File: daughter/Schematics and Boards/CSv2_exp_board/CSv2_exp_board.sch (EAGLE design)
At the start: 100 parts, among them J1 HIROSE-DF40_44-PIN_CONNECTORS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, J2 J-SERIAL-PORT, J3 CORTEX_DEBUG_SMD, J301 HIROSE-DF40_44-PIN_CONNECTORS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, J7 J-USB-HIROSE-MICRO-USB, SW1 SPST_TACT-KMR2, SW2 SPST_TACT-KMR2, U1 LOADSWITCH-MIC94164, U10 LOADSWITCH-MIC94164, U11 BMI160, U2 ADA4841-1YRJZ-R7, U205 MPL3115A2, U3 Value, U4 RFM69HCW, U5 Value, U6 Value, U7 LOADSWITCH-MIC94164, U8 LOADSWITCH-MIC94164, U9 LOADSWITCH-MIC94164, X1 32.768kHz, X2 32.768, X4 uFL

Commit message: DTR-routing 100% + DRC resolved
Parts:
- added EN_RADIO, MEAS_MIC, MEAS_RFM, MEAS_SAMD: TPTP10SQ, TestPoints:TPTP10SQ
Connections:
- net EN_RADIO: now also EN_RADIO.TP
- net MEAS_MIC: now also MEAS_MIC.TP
- net MEAS_RFM: now also MEAS_RFM.TP
- net MEAS_SAMD: now also MEAS_SAMD.TP
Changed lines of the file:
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@@
 <part name="SW1" library="adafruit" deviceset="SPST_TACT" device="-KMR2"/>
 <part name="SW2" library="adafruit" deviceset="SPST_TACT" device="-KMR2"/>
+<part name="MEAS_RFM" library="TestPoints" deviceset="TP" device="TP10SQ" package3d_urn="urn:adsk.eagle:package:27962/1" value="TPTP10SQ"/>
+<part name="MEAS_SAMD" library="TestPoints" deviceset="TP" device="TP10SQ" package3d_urn="urn:adsk.eagle:package:27962/1" value="TPTP10SQ"/>
+<part name="MEAS_MIC" library="TestPoints" deviceset="TP" device="TP10SQ" package3d_urn="urn:adsk.eagle:package:27962/1" value="TPTP10SQ"/>
+<part name="EN_RADIO" library="TestPoints" deviceset="TP" device="TP10SQ" package3d_urn="urn:adsk.eagle:package:27962/1" value="TPTP10SQ"/>
 </parts>
 <sheets>
@@
 <attribute name="VALUE" x="184.15" y="227.965" size="1.778" layer="96" rot="R270"/>
 </instance>
+<instance part="MEAS_RFM" gate="G$1" x="205.74" y="101.6" smashed="yes">
+<attribute name="NAME" x="204.47" y="102.87" size="1.778" layer="95"/>
+<attribute name="TP_SIGNAL_NAME" x="207.01" y="100.33" size="1.778" layer="97"/>
+</instance>
+<instance part="MEAS_SAMD" gate="G$1" x="208.28" y="99.06" smashed="yes">
+<attribute name="NAME" x="207.01" y="100.33" size="1.778" layer="95"/>
+<attribute name="TP_SIGNAL_NAME" x="209.55" y="97.79" size="1.778" layer="97"/>
+</instance>
+<instance part="MEAS_MIC" gate="G$1" x="203.2" y="91.44" smashed="yes">
+<attribute name="NAME" x="201.93" y="92.71" size="1.778" layer="95"/>
+<attribute name="TP_SIGNAL_NAME" x="204.47" y="90.17" size="1.778" layer="97"/>
+</instance>
+<instance part="EN_RADIO" gate="G$1" x="205.74" y="88.9" smashed="yes">
+<attribute name="NAME" x="204.47" y="90.17" size="1.778" layer="95"/>
+<attribute name="TP_SIGNAL_NAME" x="207.01" y="87.63" size="1.778" layer="97"/>
+</instance>
 </instances>
 <busses>
@@
 <wire x1="203.2" y1="88.9" x2="185.42" y2="88.9" width="0.1524" layer="91"/>
 <junction x="185.42" y="88.9"/>
+<pinref part="MEAS_MIC" gate="G$1" pin="TP"/>
 </segment>
 </net>
@@
 <wire x1="208.28" y1="96.52" x2="177.8" y2="96.52" width="0.1524" layer="91"/>
 <junction x="177.8" y="96.52"/>
+<pinref part="MEAS_SAMD" gate="G$1" pin="TP"/>
 </segment>
 </net>
@@
 <wire x1="205.74" y1="99.06" x2="175.26" y2="99.06" width="0.1524" layer="91"/>
 <junction x="175.26" y="99.06"/>
+<pinref part="MEAS_RFM" gate="G$1" pin="TP"/>
 </segment>
 </net>
@@
 <wire x1="205.74" y1="86.36" x2="187.96" y2="86.36" width="0.1524" layer="91"/>
 <junction x="187.96" y="86.36"/>
+<pinref part="EN_RADIO" gate="G$1" pin="TP"/>
 </segment>
 </net>
@@
 </segment>
 </net>
-<net name="+3V3_DTR" class="3">
+<net name="+3V3_DTR" class="0">
 <segment>
 <pinref part="J301" gate="G$1" pin="4"/>

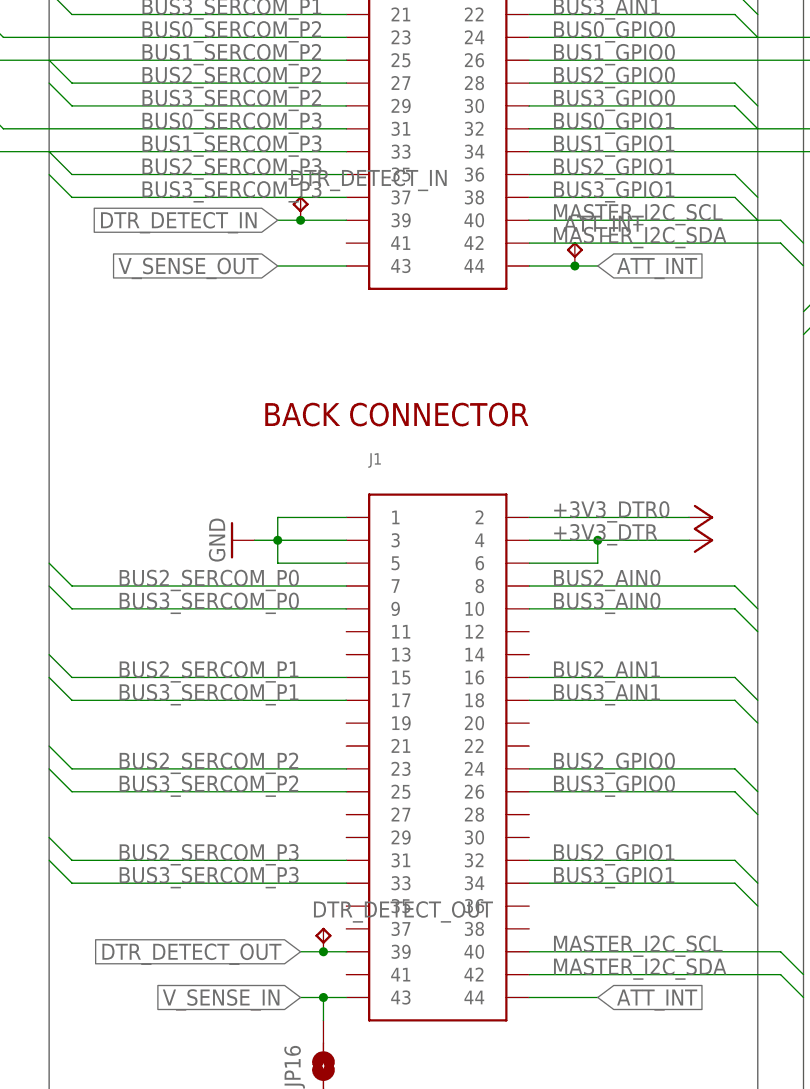
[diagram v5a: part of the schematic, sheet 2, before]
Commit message: DTR-added text/labels
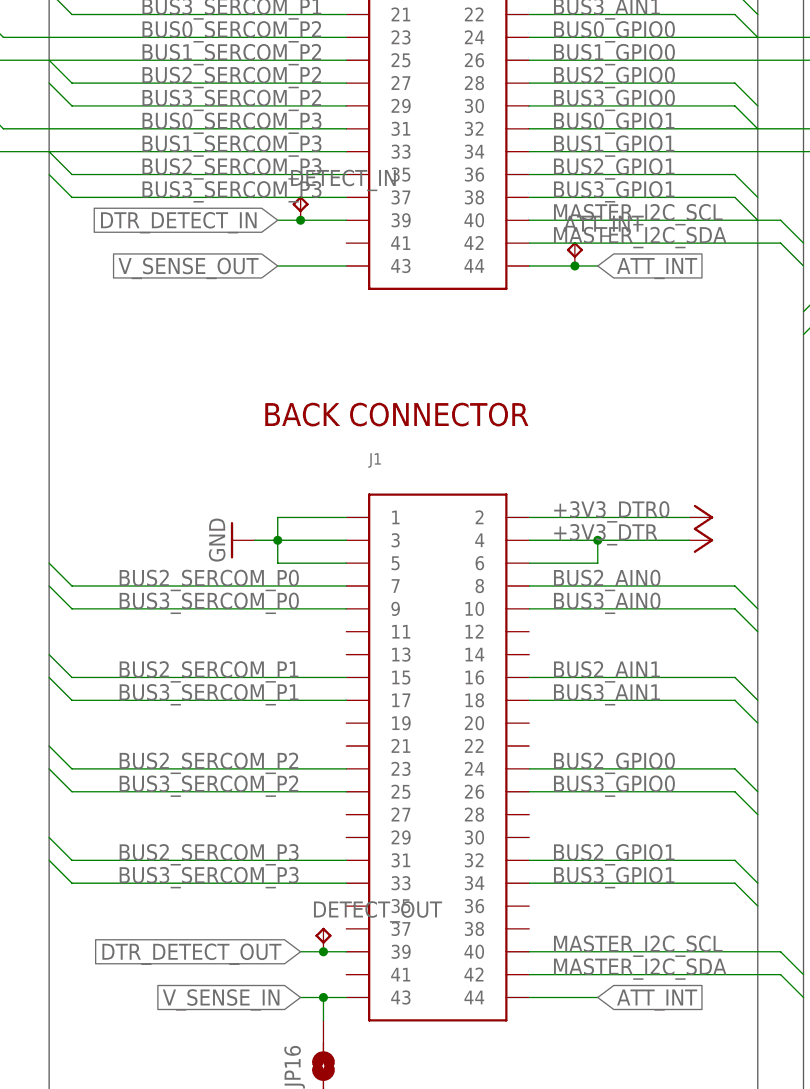
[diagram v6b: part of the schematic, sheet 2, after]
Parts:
- renumbered DTR_DETECT_IN to DETECT_IN, DTR_DETECT_OUT to DETECT_OUT
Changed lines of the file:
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@@
 <part name="JP16" library="Connectors" deviceset="JUMPER-SMT_2_NO_PASTEFREE" device=""/>
 <part name="GND25" library="Supplies" deviceset="GND" device=""/>
-<part name="DTR_DETECT_IN" library="TestPoints" deviceset="TP" device="TP10SQ" package3d_urn="urn:adsk.eagle:package:27962/1" value="TPTP10SQ"/>
+<part name="DETECT_IN" library="TestPoints" deviceset="TP" device="TP10SQ" package3d_urn="urn:adsk.eagle:package:27962/1" value="TPTP10SQ"/>
 <part name="ATT_INT" library="TestPoints" deviceset="TP" device="TP10SQ" package3d_urn="urn:adsk.eagle:package:27962/1" value="TPTP10SQ"/>
-<part name="DTR_DETECT_OUT" library="TestPoints" deviceset="TP" device="TP10SQ" package3d_urn="urn:adsk.eagle:package:27962/1" value="TPTP10SQ"/>
+<part name="DETECT_OUT" library="TestPoints" deviceset="TP" device="TP10SQ" package3d_urn="urn:adsk.eagle:package:27962/1" value="TPTP10SQ"/>
 <part name="ATT_SCL" library="TestPoints" deviceset="TP" device="TP10SQ" package3d_urn="urn:adsk.eagle:package:27962/1" value="TPTP10SQ"/>
 <part name="ATT_SDA" library="TestPoints" deviceset="TP" device="TP10SQ" package3d_urn="urn:adsk.eagle:package:27962/1" value="TPTP10SQ"/>
@@
 <attribute name="VALUE" x="292.1" y="48.26" size="1.778" layer="96"/>
 </instance>
-<instance part="DTR_DETECT_IN" gate="G$1" x="292.1" y="157.48" smashed="yes">
+<instance part="DETECT_IN" gate="G$1" x="292.1" y="157.48" smashed="yes">
 <attribute name="NAME" x="290.83" y="158.75" size="1.778" layer="95"/>
 <attribute name="TP_SIGNAL_NAME" x="293.37" y="156.21" size="1.778" layer="97"/>
@@
 <attribute name="TP_SIGNAL_NAME" x="323.85" y="151.13" size="1.778" layer="97"/>
 </instance>
-<instance part="DTR_DETECT_OUT" gate="G$1" x="294.64" y="76.2" smashed="yes">
+<instance part="DETECT_OUT" gate="G$1" x="294.64" y="76.2" smashed="yes">
 <attribute name="NAME" x="293.37" y="77.47" size="1.778" layer="95"/>
 <attribute name="TP_SIGNAL_NAME" x="295.91" y="74.93" size="1.778" layer="97"/>
@@
 <wire x1="297.18" y1="154.94" x2="292.1" y2="154.94" width="0.1524" layer="91"/>
 <label x="289.56" y="154.94" size="1.778" layer="95" rot="R180" xref="yes"/>
-<pinref part="DTR_DETECT_IN" gate="G$1" pin="TP"/>
+<pinref part="DETECT_IN" gate="G$1" pin="TP"/>
 <wire x1="292.1" y1="154.94" x2="289.56" y2="154.94" width="0.1524" layer="91"/>
 <junction x="292.1" y="154.94"/>
@@
 <wire x1="297.18" y1="73.66" x2="294.64" y2="73.66" width="0.1524" layer="91"/>
 <label x="292.1" y="73.66" size="1.778" layer="95" rot="R180" xref="yes"/>
-<pinref part="DTR_DETECT_OUT" gate="G$1" pin="TP"/>
+<pinref part="DETECT_OUT" gate="G$1" pin="TP"/>
 <wire x1="294.64" y1="73.66" x2="292.1" y2="73.66" width="0.1524" layer="91"/>
 <junction x="294.64" y="73.66"/>

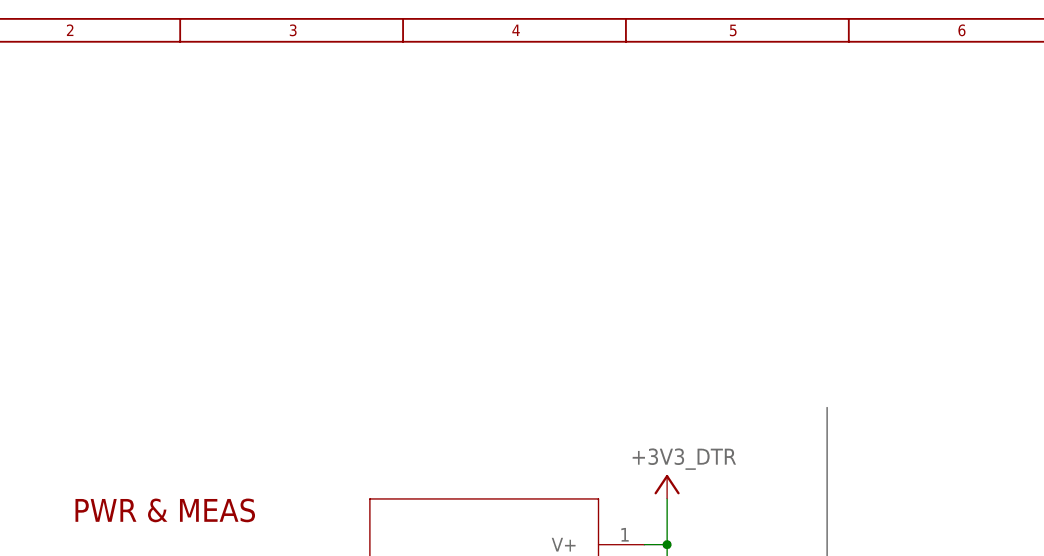
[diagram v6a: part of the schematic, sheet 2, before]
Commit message: DTR-added three ufl connectors for rf calibratiion
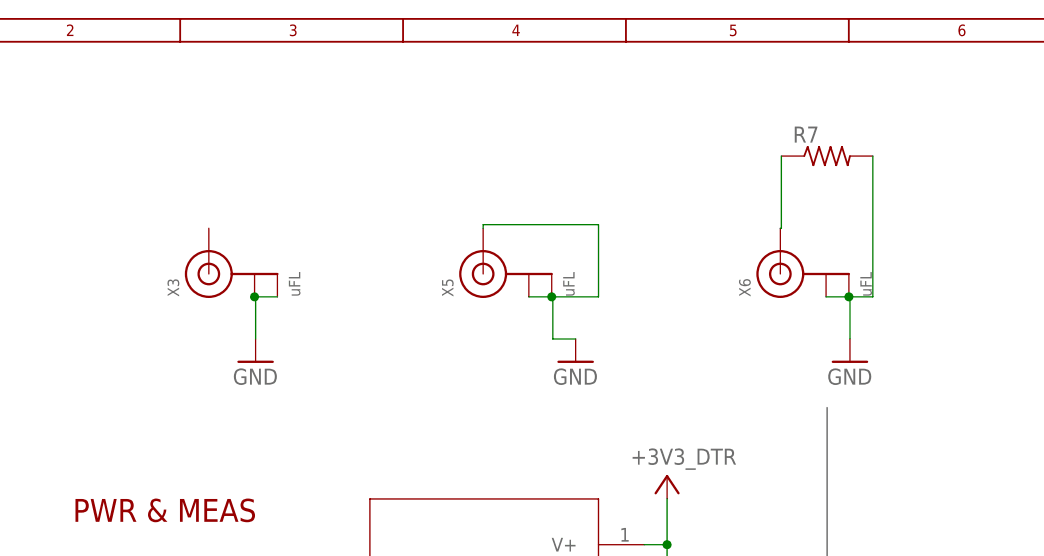
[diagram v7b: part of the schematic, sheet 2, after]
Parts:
- added R7: (no value), Resistors:R-0603
- added X3, X5, X6: uFL, Connectors:J-U.FL
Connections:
- new net N$11: R7.1, X6.SIGNAL
- net GND: now also R7.2, X3.GND@0, X3.GND@1, X5.GND@0, X5.GND@1, X5.SIGNAL, X6.GND@0, X6.GND@1
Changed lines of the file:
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@@
 <part name="MEAS_MIC" library="TestPoints" deviceset="TP" device="TP10SQ" package3d_urn="urn:adsk.eagle:package:27962/1" value="TPTP10SQ"/>
 <part name="EN_RADIO" library="TestPoints" deviceset="TP" device="TP10SQ" package3d_urn="urn:adsk.eagle:package:27962/1" value="TPTP10SQ"/>
+<part name="X3" library="Connectors" deviceset="J-U.FL" device="" value="uFL"/>
+<part name="X5" library="Connectors" deviceset="J-U.FL" device="" value="uFL"/>
+<part name="X6" library="Connectors" deviceset="J-U.FL" device="" value="uFL"/>
+<part name="R7" library="Resistors" deviceset="R-" device="0603"/>
+<part name="GND26" library="Supplies" deviceset="GND" device=""/>
+<part name="GND27" library="Supplies" deviceset="GND" device=""/>
+<part name="GND28" library="Supplies" deviceset="GND" device=""/>
 </parts>
 <sheets>
@@
 <attribute name="TP_SIGNAL_NAME" x="369.57" y="146.05" size="1.778" layer="97"/>
 </instance>
+<instance part="X3" gate="G$1" x="53.22295625" y="245.977171875" smashed="yes" rot="R90">
+<attribute name="NAME" x="49.92095625" y="243.437171875" size="1.27" layer="95" rot="R90"/>
+<attribute name="VALUE" x="63.38295625" y="243.437171875" size="1.27" layer="96" rot="R90"/>
+</instance>
+<instance part="X5" gate="G$1" x="83.70295625" y="245.977171875" smashed="yes" rot="R90">
+<attribute name="NAME" x="80.40095625" y="243.437171875" size="1.27" layer="95" rot="R90"/>
+<attribute name="VALUE" x="93.86295625" y="243.437171875" size="1.27" layer="96" rot="R90"/>
+</instance>
+<instance part="X6" gate="G$1" x="116.72295625" y="245.977171875" smashed="yes" rot="R90">
+<attribute name="NAME" x="113.42095625" y="243.437171875" size="1.27" layer="95" rot="R90"/>
+<attribute name="VALUE" x="126.88295625" y="243.437171875" size="1.27" layer="96" rot="R90"/>
+</instance>
+<instance part="R7" gate="G$1" x="121.92" y="259.08" smashed="yes">
+<attribute name="NAME" x="118.11" y="260.5786" size="1.778" layer="95"/>
+<attribute name="VALUE" x="118.11" y="255.778" size="1.778" layer="96"/>
+</instance>
+<instance part="GND26" gate="1" x="58.42" y="236.22" smashed="yes">
+<attribute name="VALUE" x="55.88" y="233.68" size="1.778" layer="96"/>
+</instance>
+<instance part="GND27" gate="1" x="93.98" y="236.22" smashed="yes">
+<attribute name="VALUE" x="91.44" y="233.68" size="1.778" layer="96"/>
+</instance>
+<instance part="GND28" gate="1" x="124.46" y="236.22" smashed="yes">
+<attribute name="VALUE" x="121.92" y="233.68" size="1.778" layer="96"/>
+</instance>
 </instances>
 <busses>
@@
 <pinref part="JP16" gate="G$1" pin="1"/>
 <wire x1="294.64" y1="53.34" x2="294.64" y2="55.88" width="0.1524" layer="91"/>
+</segment>
+<segment>
+<pinref part="X3" gate="G$1" pin="GND@1"/>
+<pinref part="X3" gate="G$1" pin="GND@0"/>
+<wire x1="60.84295625" y1="243.437171875" x2="58.30295625" y2="243.437171875" width="0.1524" layer="91"/>
+<pinref part="GND26" gate="1" pin="GND"/>
+<wire x1="58.30295625" y1="243.437171875" x2="58.42" y2="243.437171875" width="0.1524" layer="91"/>
+<wire x1="58.42" y1="243.437171875" x2="58.42" y2="238.76" width="0.1524" layer="91"/>
+<junction x="58.30295625" y="243.437171875"/>
+</segment>
+<segment>
+<pinref part="X5" gate="G$1" pin="GND@0"/>
+<pinref part="X5" gate="G$1" pin="GND@1"/>
+<wire x1="88.78295625" y1="243.437171875" x2="91.32295625" y2="243.437171875" width="0.1524" layer="91"/>
+<wire x1="91.32295625" y1="243.437171875" x2="96.52" y2="243.437171875" width="0.1524" layer="91"/>
+<junction x="91.32295625" y="243.437171875"/>
+<wire x1="96.52" y1="243.437171875" x2="96.52" y2="251.46" width="0.1524" layer="91"/>
+<pinref part="X5" gate="G$1" pin="SIGNAL"/>
+<wire x1="96.52" y1="251.46" x2="83.70295625" y2="251.46" width="0.1524" layer="91"/>
+<wire x1="83.70295625" y1="251.46" x2="83.70295625" y2="251.057171875" width="0.1524" layer="91"/>
+<wire x1="91.32295625" y1="243.437171875" x2="91.44" y2="243.437171875" width="0.1524" layer="91"/>
+<wire x1="91.44" y1="243.437171875" x2="91.44" y2="238.76" width="0.1524" layer="91"/>
+<pinref part="GND27" gate="1" pin="GND"/>
+<wire x1="91.44" y1="238.76" x2="93.98" y2="238.76" width="0.1524" layer="91"/>
+</segment>
+<segment>
+<pinref part="R7" gate="G$1" pin="2"/>
+<wire x1="127" y1="259.08" x2="127" y2="243.437171875" width="0.1524" layer="91"/>
+<pinref part="X6" gate="G$1" pin="GND@0"/>
+<wire x1="127" y1="243.437171875" x2="124.34295625" y2="243.437171875" width="0.1524" layer="91"/>
+<pinref part="X6" gate="G$1" pin="GND@1"/>
+<wire x1="124.34295625" y1="243.437171875" x2="121.80295625" y2="243.437171875" width="0.1524" layer="91"/>
+<junction x="124.34295625" y="243.437171875"/>
+<pinref part="GND28" gate="1" pin="GND"/>
+<wire x1="124.46" y1="238.76" x2="124.46" y2="243.437171875" width="0.1524" layer="91"/>
+<wire x1="124.46" y1="243.437171875" x2="124.34295625" y2="243.437171875" width="0.1524" layer="91"/>
 </segment>
 </net>
@@
 </segment>
 </net>
+<net name="N$11" class="0">
+<segment>
+<pinref part="X6" gate="G$1" pin="SIGNAL"/>
+<pinref part="R7" gate="G$1" pin="1"/>
+<wire x1="116.72295625" y1="251.057171875" x2="116.84" y2="251.057171875" width="0.1524" layer="91"/>
+<wire x1="116.84" y1="251.057171875" x2="116.84" y2="259.08" width="0.1524" layer="91"/>
+</segment>
+</net>

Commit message: DTR-added codec datasheet and did replacement
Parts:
- removed EN_MEAS, MEAS_RFM: TPTP10SQ, TestPoints:TPTP10SQ
- added C26, C27, C28: (no value), CommonSense-DTR-v1:C0402-ANT0402
- added C29: 1u, Capacitors:C-0402
- added C30: 100n, Capacitors:C-0402
- added C31, C32, C33: (no value), Capacitors:C-0402
- added C34, C36, C38: 0.1u, Capacitors:C-0402
- added C35, C37, C39: 10u, Capacitors:C-0402
- added J4: SJ-43514-SMT, CommonSense-DTR-v1:SJ-43514-SMT
- added JP15, JP17: JUMPER-SMT_2_NC_PASTELG_NO-SILK, Connectors:JUMPER-SMT_2_NC_PASTELG_NO-SILK
- added L1: L0402, Inductors:L0402
- added R10, R11, R9: 100k, Resistors:R-0402
- added R12, R8: (no value), Resistors:R-0402
- added TP1: TPTP11SQ, TestPoints:TPTP11SQ
- added U12: TLV320DAC26IRHB, CommonSense-DTR-v1:TLV320DAC26IRHB
- added U13: ADG839YKSZ-500RL7KS_6_ADI-L, CommonSense-DTR-v1:ADG839YKSZ-500RL7KS_6_ADI-L
- added U14: LOADSWITCH-MIC94164, Switches:LOADSWITCH-MIC94164
- C1, C12, C14, C2, C203, C204, C3-4.7N, C4, C6, C7, C8: device Capacitors:C-0603 -> Capacitors:C-0402
- C9: device Capacitors:C-0805 -> Capacitors:C-0402
- R1, R1-100K, R2, R3, R3-39R, R4, R5, R6, R7, R_SENSE: device Resistors:R-0603 -> Resistors:R-0402
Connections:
- new net +3V3_CODEC: C34.1, C35.1, C36.1, C37.1, JP15.2, R11.2, R9.2, U12.AVDD, U12.DRVDD, U12.IOVDD
- new net +3V3_CODEC_IN: C29.1, JP17.2, U14.VIN
- new net +3V3_CODEC_OUT: C30.1, JP15.1, U14.VOUT
- new net +3V3_CODEC_PWR: JP17.1, U3.COM1
- new net AGND: C31.2, C36.2, C37.2, J4.RING2, J4.TIP, R12.1, U12.AVSS, U12.DRVSS
- new net CODEC_!RESET: R11.1, TP1.TP, U12.!RESET
- new net EN_CODEC: ATTINY-817.PC4, U14.ENABLE
- new net MEAS_CODEC: ATTINY-817.PC3, U3.IN1
- new net N$13: C26.2, C27.1, L1.1
- new net N$14: R8.1, U12.MICBIAS
- new net N$15: C31.1, U12.HPL
- new net N$16: C32.2, J4.RING1
- new net N$21: C38.1, C39.1, R10.1, R9.1, U12.DVDD
- new net N$25: C32.1, U12.HPR
- new net N$27: C33.1, U12.MICIN
- new net N$28: C33.2, J4.SLEEVE, R8.2
- new net N$9: C26.1, SJ3.1
- net +3V3_DTR: now also U13.VDD
- net +3V3_MEAS: now also U13.S2
- net +3V3_NMEAS: now also U3.NC1
- net BUS0_AIN0: now also ATTINY-817.PA1; no longer R2.1, U2.VOUT
- net BUS0_GPIO0: now also U$4.PA15/I15/SERCOM3+4.3; no longer ATTINY-817.PA1, U$4.PA14/I14/SERCOM2+4.2
- net BUS0_GPIO1: now also U12.!SS; no longer U$4.PA15/I15/SERCOM3+4.3
- net BUS0_SERCOM_P0: now also U12.MISO
- net BUS0_SERCOM_P1: now also U12.SCLK
- net BUS0_SERCOM_P3: now also U12.MOSI
- net BUS1_AIN0: now also R2.1, U2.VOUT
- net EN_MEAS: now also U13.IN; no longer EN_MEAS.TP, U3.IN1
- net GND: now also C27.2, C28.1, C28.2, C29.2, C30.2, C34.2, C35.2, C38.2, C39.2, L1.2, R10.2, R12.2, U12.DVSS, U13.GND, U14.GND; no longer SJ3.1
- net MEAS_RFM: no longer MEAS_RFM.TP
- net V_SENSE_IN: now also U13.S1; no longer U3.NC1
- net V_SENSE_OUT: now also U13.D; no longer U3.COM1
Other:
- moved on the sheet: C10, C11, C17, C18, C19, C20, C21, C22, C23, C24, C3, C5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
